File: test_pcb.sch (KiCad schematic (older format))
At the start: 27 parts, among them J1 Conn_01x04_Male, J10 Conn_01x20_Female, J11 Conn_01x20_Female, J12 Power out, J13 Power in, J14 SRF2, J15 SRF1, J16 IR1, J17 IR2, J18 I2C2, J19 I2C1, J2 on/off, J20 A2, J21 A3, J22 Keypad, J23 ENCB, J24 ENCA, J25 MC1-2A, J26 MC1-2B, J3 LED, J4 Power, J5 Power, J6 Servo1, J7 Servo2, J8 Motors, J9 MC2, SW1 on/off

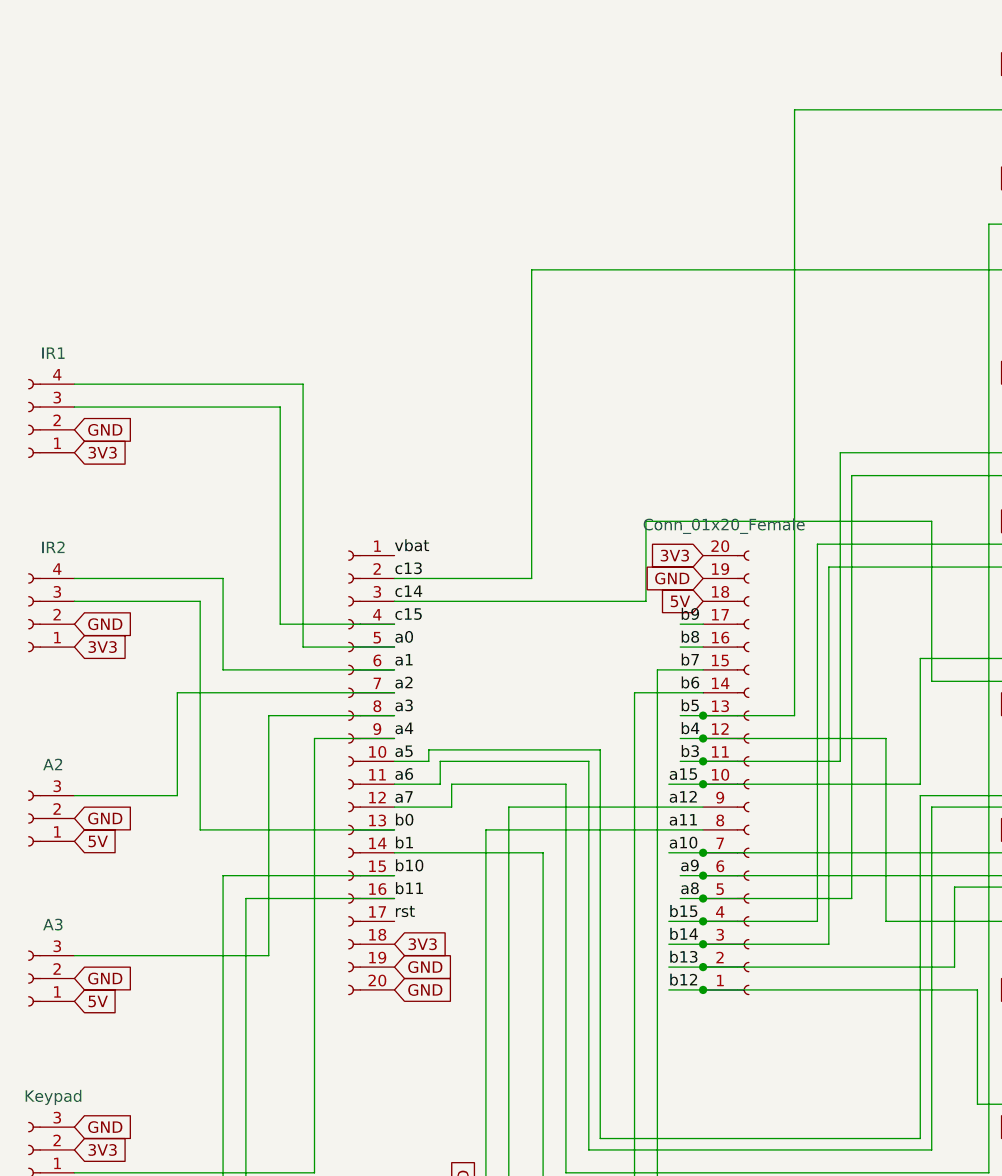
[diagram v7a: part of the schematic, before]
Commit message: changes in eeschema
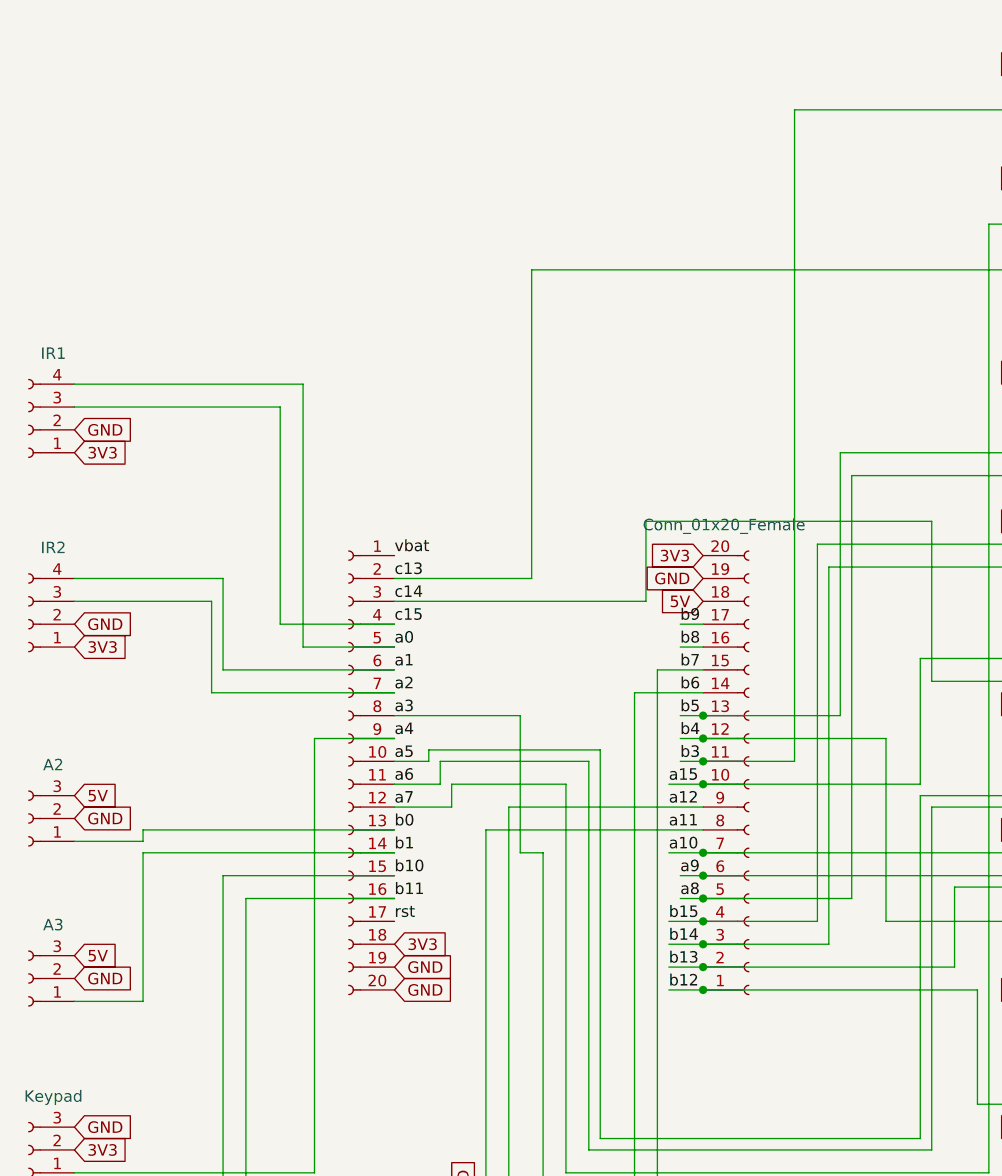
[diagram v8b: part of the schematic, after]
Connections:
- net 5V: now also J20.3 (Pin_3), J21.3 (Pin_3); no longer J20.1 (Pin_1), J21.1 (Pin_1)
- net a2: now also J17.3 (Pin_3); no longer J20.3 (Pin_3)
- net a3: now also J9.1 (Pin_1); no longer J21.3 (Pin_3)
- net b0: now also J20.1 (Pin_1); no longer J17.3 (Pin_3)
- net b1: now also J21.1 (Pin_1); no longer J9.1 (Pin_1)
- net b3: now also J6.3 (Pin_3); no longer J25.1 (Pin_1), J8.1 (Pin_1)
- net b5: now also J25.1 (Pin_1), J8.1 (Pin_1); no longer J6.3 (Pin_3)
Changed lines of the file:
@@
 	8150 3300 8250 3300
 Wire Wire Line
-	1150 5050 2000 5050
-Wire Wire Line
-	2000 5050 2000 4000
-Wire Wire Line
-	1150 4350 1600 4350
-Wire Wire Line
-	1600 4350 1600 3900
-Wire Wire Line
 	1150 3400 1800 3400
-Wire Wire Line
-	2000 4000 2550 4000
-Wire Wire Line
-	1600 3900 2550 3900
 Wire Wire Line
 	1800 3400 1800 3800
@@
 Text GLabel 1150 5150 2    50   Input ~ 0
 GND
-Text GLabel 1150 4450 2    50   Input ~ 0
-GND
 Text GLabel 1150 3600 2    50   Input ~ 0
 GND
@@
 	1150 6000 2200 6000
 Wire Wire Line
-	1700 3500 1700 4500
-Wire Wire Line
-	1150 3500 1700 3500
-Wire Wire Line
-	1700 4500 2550 4500
-Wire Wire Line
 	3800 4100 3900 4100
 Wire Wire Line
@@
 $EndComp
 Wire Wire Line
-	4300 1350 4300 4000
-Wire Wire Line
 	5450 2850 4500 2850
 Wire Wire Line
@@
 	4900 4400 5450 4400
 Wire Wire Line
-	2550 4200 2700 4200
-Wire Wire Line
-	2700 4200 2700 4150
-Wire Wire Line
-	2700 4150 3450 4150
-Wire Wire Line
-	3450 4150 3450 5850
-Wire Wire Line
-	3450 5850 4850 5850
-Wire Wire Line
-	4850 5850 4850 4350
-Wire Wire Line
-	4850 4350 5250 4350
-Wire Wire Line
-	5250 4350 5250 4300
-Wire Wire Line
-	5250 4300 5450 4300
-Wire Wire Line
-	2550 4600 3200 4600
-Wire Wire Line
 	3200 4600 3200 6150
 Wire Wire Line
@@
 Wire Wire Line
 	3800 3700 3900 3700
-Text GLabel 1150 5250 2    50   Input ~ 0
-5V
-Text GLabel 1150 4550 2    50   Input ~ 0
-5V
 Connection ~ 3900 4300
 Connection ~ 3900 4600
@@
 	3750 4600 3900 4600
 Wire Wire Line
-	4850 4300 3900 4300
-Wire Wire Line
 	3750 4300 3900 4300
-Connection ~ 3900 4000
-Connection ~ 3900 4200
 Wire Wire Line
 	3900 5200 5100 5200
@@
 	3800 4000 3900 4000
 Wire Wire Line
-	4300 4000 3900 4000
-Wire Wire Line
 	3750 4900 3900 4900
 Wire Wire Line
@@
 	3800 4200 3900 4200
 Wire Wire Line
-	4500 4200 3900 4200
-Wire Wire Line
 	3700 3800 3700 7050
 Wire Wire Line
 	3600 3900 3600 7150
-Wire Wire Line
-	4500 2850 4500 4200
 Wire Wire Line
 	4400 3250 4400 4900
@@
 Text GLabel 6650 4350 0    50   Input ~ 0
 GND
+Text GLabel 1150 4450 2    50   Input ~ 0
+GND
+Wire Wire Line
+	4850 4300 3900 4300
+Wire Wire Line
+	2550 4200 2700 4200
+Wire Wire Line
+	2700 4200 2700 4150
+Wire Wire Line
+	2700 4150 3450 4150
+Wire Wire Line
+	3450 5850 4850 5850
+Wire Wire Line
+	3450 4150 3450 5850
+Wire Wire Line
+	4500 2850 4500 4000
+Wire Wire Line
+	1150 3500 1750 3500
+Wire Wire Line
+	1750 3500 1750 3900
+Wire Wire Line
+	1750 3900 2550 3900
+Text GLabel 1150 4350 2    50   Input ~ 0
+5V
+Text GLabel 1150 5050 2    50   Input ~ 0
+5V
+Wire Wire Line
+	2550 4500 1450 4500
+Wire Wire Line
+	1450 4500 1450 4550
+Wire Wire Line
+	1450 4550 1150 4550
+Wire Wire Line
+	3200 4600 3100 4600
+Wire Wire Line
+	3100 4600 3100 4000
+Wire Wire Line
+	3100 4000 2550 4000
+Wire Wire Line
+	2550 4600 1450 4600
+Wire Wire Line
+	1450 4600 1450 5250
+Wire Wire Line
+	1450 5250 1150 5250
+Connection ~ 3900 4200
+Wire Wire Line
+	4850 5850 4850 4350
+Wire Wire Line
+	5250 4350 5250 4300
+Wire Wire Line
+	4850 4350 5250 4350
+Wire Wire Line
+	5250 4300 5450 4300
+Wire Wire Line
+	4300 4200 3900 4200
+Wire Wire Line
+	4300 1350 4300 4200
+Wire Wire Line
+	3900 4000 4500 4000
+Connection ~ 3900 4000
 $EndSCHEMATC
